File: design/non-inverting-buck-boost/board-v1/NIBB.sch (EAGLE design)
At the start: 0 parts

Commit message: added switches
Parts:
- added D1, D2: MUR820, diode:MUR820
- added L1: RKE16, inductors:RKE16
- added Q1, Q2: IRLZ44Z, transistor-power:IRLZ44Z
- added U$1: ZXGD3006E6, felippe:ZXGD3006E6
- added VIN: 2PIN, con-molex:22-23-2021
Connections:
- new net N$1: D1.C, L1.1, Q1.S
- new net N$2: L1.2, Q2.D
- new net N$3: Q1.D, VIN-1.S
- new net N$4: D1.A, Q2.S, VIN-2.S

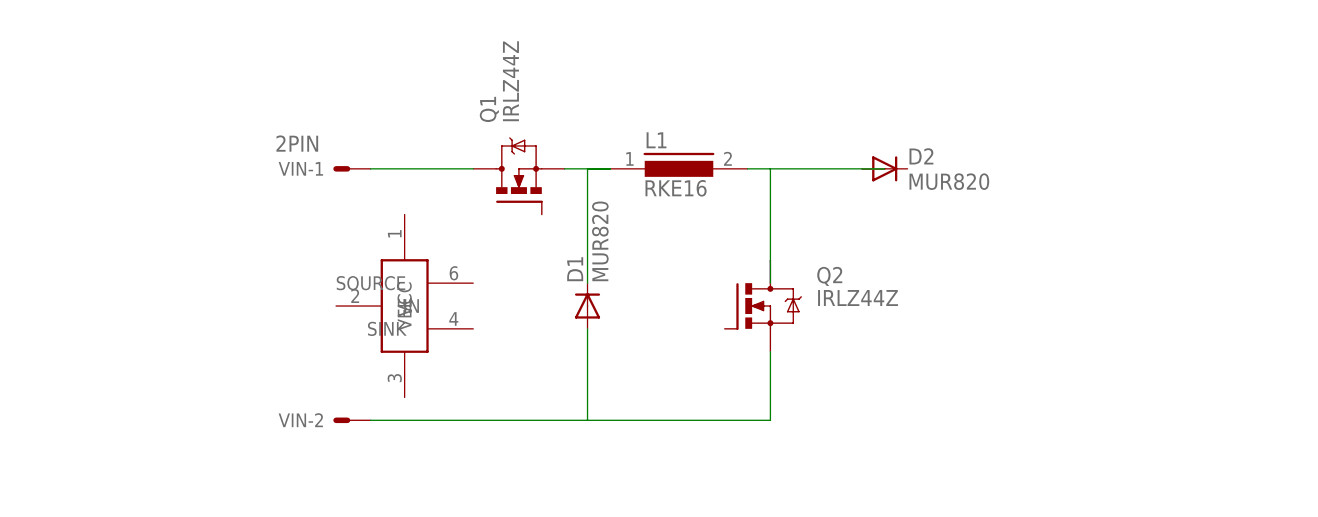
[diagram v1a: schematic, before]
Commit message: added connectors
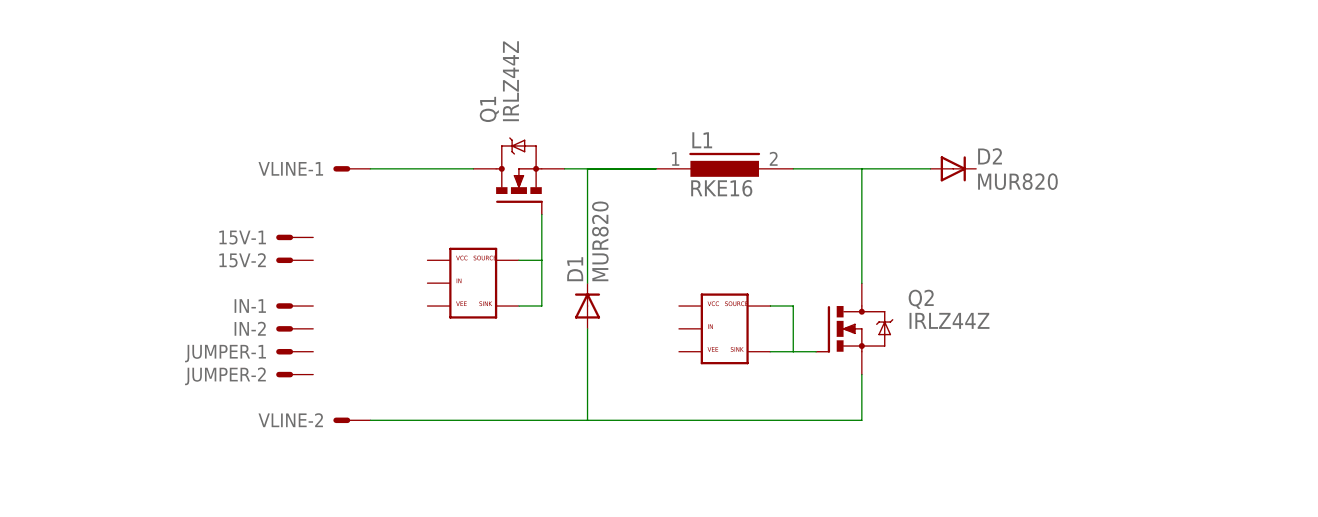
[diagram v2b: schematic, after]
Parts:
- added 15V, IN, JUMPER: 22-23-2021, con-molex:22-23-2021
- added U$2: ZXGD3006E6, felippe:ZXGD3006E6
- VLINE: value 2PIN -> 22-23-2021
- renumbered VIN to VLINE
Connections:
- new net N$5: Q1.G, U$1.SINK, U$1.SOURCE
- new net N$6: Q2.G, U$2.SINK, U$2.SOURCE
- net N$2: now also D2.A
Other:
- moved on the sheet: D2, L1, Q2
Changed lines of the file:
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@@
 <part name="L1" library="inductors" deviceset="RKE16" device=""/>
 <part name="Q2" library="transistor-power" deviceset="IRLZ44Z" device=""/>
-<part name="VIN" library="con-molex" deviceset="22-23-2021" device="" value="2PIN"/>
+<part name="VLINE" library="con-molex" deviceset="22-23-2021" device="" value=""/>
 <part name="U$1" library="felippe" deviceset="ZXGD3006E6" device=""/>
+<part name="U$2" library="felippe" deviceset="ZXGD3006E6" device=""/>
+<part name="15V" library="con-molex" deviceset="22-23-2021" device="" value=""/>
+<part name="IN" library="con-molex" deviceset="22-23-2021" device="" value=""/>
+<part name="JUMPER" library="con-molex" deviceset="22-23-2021" device="" value=""/>
 </parts>
 <sheets>
@@
 <instances>
 <instance part="D1" gate="1" x="25.4" y="48.26" rot="R90"/>
-<instance part="D2" gate="1" x="58.42" y="63.5"/>
+<instance part="D2" gate="1" x="66.04" y="63.5"/>
 <instance part="Q1" gate="G$1" x="17.78" y="60.96" rot="R90"/>
-<instance part="L1" gate="1" x="35.56" y="63.5"/>
-<instance part="Q2" gate="G$1" x="43.18" y="48.26"/>
-<instance part="VIN" gate="-1" x="-1.27" y="63.5" smashed="yes" rot="R180">
-<attribute name="NAME" x="-3.81" y="64.262" size="1.524" layer="95" rot="R180"/>
-<attribute name="VALUE" x="-4.318" y="67.183" size="1.778" layer="96" rot="R180"/>
+<instance part="L1" gate="1" x="40.64" y="63.5"/>
+<instance part="Q2" gate="G$1" x="53.34" y="45.72"/>
+<instance part="VLINE" gate="-1" x="-1.27" y="63.5" rot="R180"/>
+<instance part="VLINE" gate="-2" x="-1.27" y="35.56" rot="R180"/>
+<instance part="U$1" gate="G$1" x="12.7" y="50.8"/>
+<instance part="U$2" gate="G$1" x="40.64" y="45.72"/>
+<instance part="15V" gate="-1" x="-7.62" y="55.88" smashed="yes" rot="R180">
+<attribute name="NAME" x="-10.16" y="56.642" size="1.524" layer="95" rot="R180"/>
+<attribute name="VALUE" x="-11.938" y="59.563" size="1.778" layer="96" rot="R180"/>
 </instance>
-<instance part="VIN" gate="-2" x="-1.27" y="35.56" rot="R180"/>
-<instance part="U$1" gate="G$1" x="5.08" y="48.26"/>
+<instance part="15V" gate="-2" x="-7.62" y="53.34" rot="R180"/>
+<instance part="IN" gate="-1" x="-7.62" y="48.26" smashed="yes" rot="R180">
+<attribute name="NAME" x="-10.16" y="49.022" size="1.524" layer="95" rot="R180"/>
+<attribute name="VALUE" x="-11.938" y="51.943" size="1.778" layer="96" rot="R180"/>
+</instance>
+<instance part="IN" gate="-2" x="-7.62" y="45.72" rot="R180"/>
+<instance part="JUMPER" gate="-1" x="-7.62" y="43.18" rot="R180"/>
+<instance part="JUMPER" gate="-2" x="-7.62" y="40.64" rot="R180"/>
 </instances>
 <busses>
@@
 <pinref part="Q1" gate="G$1" pin="S"/>
 <pinref part="L1" gate="1" pin="1"/>
-<wire x1="22.86" y1="63.5" x2="27.94" y2="63.5" width="0.1524" layer="91"/>
-<wire x1="27.94" y1="63.5" x2="25.4" y2="63.5" width="0.1524" layer="91"/>
+<wire x1="22.86" y1="63.5" x2="33.02" y2="63.5" width="0.1524" layer="91"/>
+<wire x1="33.02" y1="63.5" x2="25.4" y2="63.5" width="0.1524" layer="91"/>
 <wire x1="25.4" y1="63.5" x2="25.4" y2="50.8" width="0.1524" layer="91"/>
 <pinref part="D1" gate="1" pin="C"/>
@@
 <segment>
 <pinref part="Q2" gate="G$1" pin="D"/>
-<wire x1="45.72" y1="53.34" x2="45.72" y2="50.8" width="0.1524" layer="91"/>
 <pinref part="L1" gate="1" pin="2"/>
-<wire x1="43.18" y1="63.5" x2="45.72" y2="63.5" width="0.1524" layer="91"/>
-<wire x1="45.72" y1="63.5" x2="58.42" y2="63.5" width="0.1524" layer="91"/>
-<wire x1="45.72" y1="53.34" x2="45.72" y2="63.5" width="0.1524" layer="91"/>
+<wire x1="48.26" y1="63.5" x2="55.88" y2="63.5" width="0.1524" layer="91"/>
+<wire x1="55.88" y1="50.8" x2="55.88" y2="63.5" width="0.1524" layer="91"/>
+<pinref part="D2" gate="1" pin="A"/>
+<wire x1="55.88" y1="63.5" x2="63.5" y2="63.5" width="0.1524" layer="91"/>
 </segment>
 </net>
@@
 <segment>
 <pinref part="Q2" gate="G$1" pin="S"/>
-<wire x1="45.72" y1="43.18" x2="45.72" y2="35.56" width="0.1524" layer="91"/>
-<wire x1="45.72" y1="35.56" x2="25.4" y2="35.56" width="0.1524" layer="91"/>
+<wire x1="55.88" y1="40.64" x2="55.88" y2="35.56" width="0.1524" layer="91"/>
+<wire x1="55.88" y1="35.56" x2="25.4" y2="35.56" width="0.1524" layer="91"/>
 <pinref part="D1" gate="1" pin="A"/>
 <wire x1="25.4" y1="35.56" x2="25.4" y2="45.72" width="0.1524" layer="91"/>
-<pinref part="VIN" gate="-2" pin="S"/>
+<pinref part="VLINE" gate="-2" pin="S"/>
 <wire x1="1.27" y1="35.56" x2="25.4" y2="35.56" width="0.1524" layer="91"/>
 </segment>
@@
 <segment>
 <pinref part="Q1" gate="G$1" pin="D"/>
-<pinref part="VIN" gate="-1" pin="S"/>
+<pinref part="VLINE" gate="-1" pin="S"/>
 <wire x1="1.27" y1="63.5" x2="12.7" y2="63.5" width="0.1524" layer="91"/>
 </segment>
 </net>
+<net name="N$5" class="0">
+<segment>
+<pinref part="U$1" gate="G$1" pin="SOURCE"/>
+<wire x1="17.78" y1="53.34" x2="20.32" y2="53.34" width="0.1524" layer="91"/>
+<pinref part="Q1" gate="G$1" pin="G"/>
+<wire x1="20.32" y1="53.34" x2="20.32" y2="58.42" width="0.1524" layer="91"/>
+<pinref part="U$1" gate="G$1" pin="SINK"/>
+<wire x1="17.78" y1="48.26" x2="20.32" y2="48.26" width="0.1524" layer="91"/>
+<wire x1="20.32" y1="48.26" x2="20.32" y2="53.34" width="0.1524" layer="91"/>
+</segment>
+</net>
+<net name="N$6" class="0">
+<segment>
+<pinref part="U$2" gate="G$1" pin="SOURCE"/>
+<wire x1="48.26" y1="48.26" x2="45.72" y2="48.26" width="0.1524" layer="91"/>
+<wire x1="48.26" y1="43.18" x2="48.26" y2="48.26" width="0.1524" layer="91"/>
+<pinref part="U$2" gate="G$1" pin="SINK"/>
+<wire x1="45.72" y1="43.18" x2="48.26" y2="43.18" width="0.1524" layer="91"/>
+<pinref part="Q2" gate="G$1" pin="G"/>
+<wire x1="48.26" y1="43.18" x2="50.8" y2="43.18" width="0.1524" layer="91"/>
+</segment>
+</net>

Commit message: updated connectors
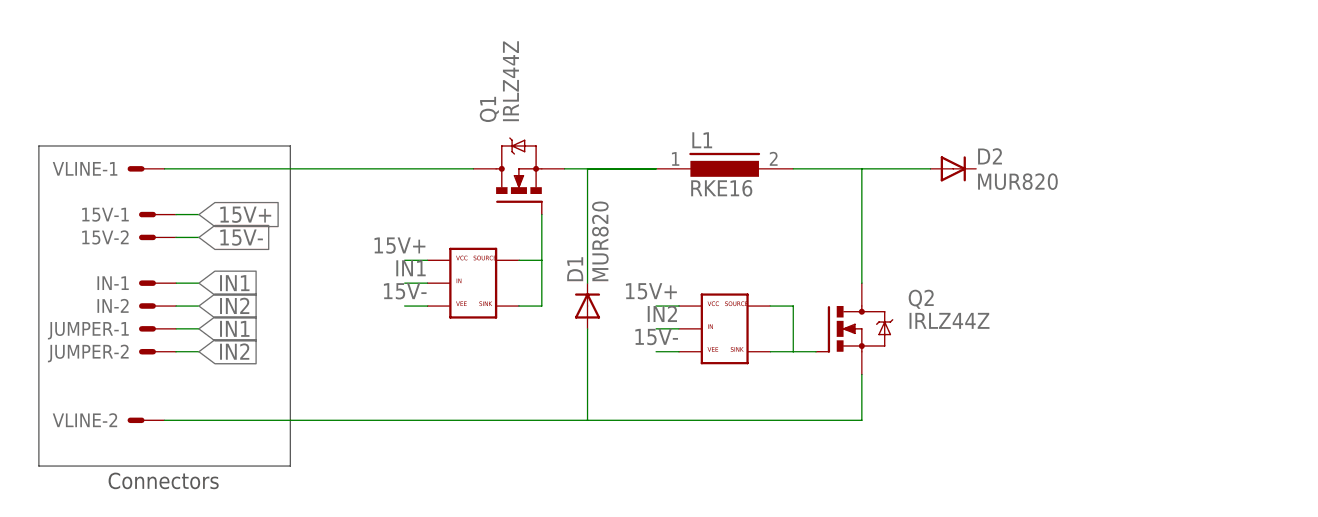
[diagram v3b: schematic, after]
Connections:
- new net 15V+: 15V-1.S, U$1.VCC, U$2.VCC
- new net 15V-: 15V-2.S, U$1.VEE, U$2.VEE
- new net IN1: IN-1.S, JUMPER-1.S, U$1.IN
- new net IN2: IN-2.S, JUMPER-2.S, U$2.IN
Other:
- note added: "Connectors"
- moved on the sheet: 15V-1, 15V-2, IN-1, IN-2, JUMPER-1, JUMPER-2, VLINE-1, VLINE-2
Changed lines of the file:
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@@
 <sheet>
 <plain>
+<text x="-27.94" y="27.94" size="1.778" layer="92">Connectors</text>
 </plain>
 <instances>
@@
 <instance part="L1" gate="1" x="40.64" y="63.5"/>
 <instance part="Q2" gate="G$1" x="53.34" y="45.72"/>
-<instance part="VLINE" gate="-1" x="-1.27" y="63.5" rot="R180"/>
-<instance part="VLINE" gate="-2" x="-1.27" y="35.56" rot="R180"/>
+<instance part="VLINE" gate="-1" x="-24.13" y="63.5" rot="R180"/>
+<instance part="VLINE" gate="-2" x="-24.13" y="35.56" rot="R180"/>
 <instance part="U$1" gate="G$1" x="12.7" y="50.8"/>
 <instance part="U$2" gate="G$1" x="40.64" y="45.72"/>
-<instance part="15V" gate="-1" x="-7.62" y="55.88" smashed="yes" rot="R180">
-<attribute name="NAME" x="-10.16" y="56.642" size="1.524" layer="95" rot="R180"/>
-<attribute name="VALUE" x="-11.938" y="59.563" size="1.778" layer="96" rot="R180"/>
+<instance part="15V" gate="-1" x="-22.86" y="58.42" smashed="yes" rot="R180">
+<attribute name="NAME" x="-25.4" y="59.182" size="1.524" layer="95" rot="R180"/>
+<attribute name="VALUE" x="-27.178" y="62.103" size="1.778" layer="96" rot="R180"/>
 </instance>
-<instance part="15V" gate="-2" x="-7.62" y="53.34" rot="R180"/>
-<instance part="IN" gate="-1" x="-7.62" y="48.26" smashed="yes" rot="R180">
-<attribute name="NAME" x="-10.16" y="49.022" size="1.524" layer="95" rot="R180"/>
-<attribute name="VALUE" x="-11.938" y="51.943" size="1.778" layer="96" rot="R180"/>
+<instance part="15V" gate="-2" x="-22.86" y="55.88" rot="R180"/>
+<instance part="IN" gate="-1" x="-22.86" y="50.8" smashed="yes" rot="R180">
+<attribute name="NAME" x="-25.4" y="51.562" size="1.524" layer="95" rot="R180"/>
+<attribute name="VALUE" x="-27.178" y="54.483" size="1.778" layer="96" rot="R180"/>
 </instance>
-<instance part="IN" gate="-2" x="-7.62" y="45.72" rot="R180"/>
-<instance part="JUMPER" gate="-1" x="-7.62" y="43.18" rot="R180"/>
-<instance part="JUMPER" gate="-2" x="-7.62" y="40.64" rot="R180"/>
+<instance part="IN" gate="-2" x="-22.86" y="48.26" rot="R180"/>
+<instance part="JUMPER" gate="-1" x="-22.86" y="45.72" rot="R180"/>
+<instance part="JUMPER" gate="-2" x="-22.86" y="43.18" rot="R180"/>
 </instances>
 <busses>
+<bus name="B$1">
+<segment>
+<wire x1="-35.56" y1="66.04" x2="-7.62" y2="66.04" width="0.762" layer="92"/>
+<wire x1="-7.62" y1="66.04" x2="-7.62" y2="30.48" width="0.762" layer="92"/>
+<wire x1="-7.62" y1="30.48" x2="-35.56" y2="30.48" width="0.762" layer="92"/>
+<wire x1="-35.56" y1="30.48" x2="-35.56" y2="66.04" width="0.762" layer="92"/>
+</segment>
+</bus>
 </busses>
 <nets>
@@
 <wire x1="25.4" y1="35.56" x2="25.4" y2="45.72" width="0.1524" layer="91"/>
 <pinref part="VLINE" gate="-2" pin="S"/>
-<wire x1="1.27" y1="35.56" x2="25.4" y2="35.56" width="0.1524" layer="91"/>
+<wire x1="-21.59" y1="35.56" x2="25.4" y2="35.56" width="0.1524" layer="91"/>
 </segment>
 </net>
@@
 <pinref part="Q1" gate="G$1" pin="D"/>
 <pinref part="VLINE" gate="-1" pin="S"/>
-<wire x1="1.27" y1="63.5" x2="12.7" y2="63.5" width="0.1524" layer="91"/>
+<wire x1="-21.59" y1="63.5" x2="12.7" y2="63.5" width="0.1524" layer="91"/>
 </segment>
 </net>
@@
 </segment>
 </net>
+<net name="15V+" class="0">
+<segment>
+<pinref part="15V" gate="-1" pin="S"/>
+<wire x1="-20.32" y1="58.42" x2="-17.78" y2="58.42" width="0.1524" layer="91"/>
+<label x="-17.78" y="58.42" size="1.778" layer="95" xref="yes"/>
+</segment>
+<segment>
+<pinref part="U$1" gate="G$1" pin="VCC"/>
+<wire x1="7.62" y1="53.34" x2="5.08" y2="53.34" width="0.1524" layer="91"/>
+<label x="7.62" y="55.88" size="1.778" layer="95" rot="R180"/>
+</segment>
+<segment>
+<pinref part="U$2" gate="G$1" pin="VCC"/>
+<wire x1="35.56" y1="48.26" x2="33.02" y2="48.26" width="0.1524" layer="91"/>
+<label x="35.56" y="50.8" size="1.778" layer="95" rot="R180"/>
+</segment>
+</net>
+<net name="15V-" class="0">
+<segment>
+<pinref part="15V" gate="-2" pin="S"/>
+<wire x1="-20.32" y1="55.88" x2="-17.78" y2="55.88" width="0.1524" layer="91"/>
+<label x="-17.78" y="55.88" size="1.778" layer="95" xref="yes"/>
+</segment>
+<segment>
+<pinref part="U$1" gate="G$1" pin="VEE"/>
+<wire x1="7.62" y1="48.26" x2="5.08" y2="48.26" width="0.1524" layer="91"/>
+<label x="7.62" y="50.8" size="1.778" layer="95" rot="R180"/>
+</segment>
+<segment>
+<pinref part="U$2" gate="G$1" pin="VEE"/>
+<wire x1="35.56" y1="43.18" x2="33.02" y2="43.18" width="0.1524" layer="91"/>
+<label x="35.56" y="45.72" size="1.778" layer="95" rot="R180"/>
+</segment>
+</net>
+<net name="IN1" class="0">
+<segment>
+<pinref part="IN" gate="-1" pin="S"/>
+<wire x1="-20.32" y1="50.8" x2="-17.78" y2="50.8" width="0.1524" layer="91"/>
+<label x="-17.78" y="50.8" size="1.778" layer="95" xref="yes"/>
+</segment>
+<segment>
+<pinref part="JUMPER" gate="-1" pin="S"/>
+<wire x1="-20.32" y1="45.72" x2="-17.78" y2="45.72" width="0.1524" layer="91"/>
+<label x="-17.78" y="45.72" size="1.778" layer="95" xref="yes"/>
+</segment>
+<segment>
+<pinref part="U$1" gate="G$1" pin="IN"/>
+<wire x1="7.62" y1="50.8" x2="5.08" y2="50.8" width="0.1524" layer="91"/>
+<label x="7.62" y="53.34" size="1.778" layer="95" rot="R180"/>
+</segment>
+</net>
+<net name="IN2" class="0">
+<segment>
+<pinref part="IN" gate="-2" pin="S"/>
+<wire x1="-20.32" y1="48.26" x2="-17.78" y2="48.26" width="0.1524" layer="91"/>
+<label x="-17.78" y="48.26" size="1.778" layer="95" xref="yes"/>
+</segment>
+<segment>
+<pinref part="JUMPER" gate="-2" pin="S"/>
+<wire x1="-20.32" y1="43.18" x2="-17.78" y2="43.18" width="0.1524" layer="91"/>
+<label x="-17.78" y="43.18" size="1.778" layer="95" xref="yes"/>
+</segment>
+<segment>
+<pinref part="U$2" gate="G$1" pin="IN"/>
+<wire x1="35.56" y1="45.72" x2="33.02" y2="45.72" width="0.1524" layer="91"/>
+<label x="35.56" y="48.26" size="1.778" layer="95" rot="R180"/>
+</segment>
+</net>

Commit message: added output capacitor and connector
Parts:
- added C1: (no value), capacitor:CAPP-UF
- added OUT: 22-23-2021, con-molex:22-23-2021
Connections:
- new net N$7: C1.+, D2.C, OUT-1.S
- net N$4: now also C1.-, OUT-2.S
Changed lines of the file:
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@@
 <part name="IN" library="con-molex" deviceset="22-23-2021" device="" value=""/>
 <part name="JUMPER" library="con-molex" deviceset="22-23-2021" device="" value=""/>
+<part name="C1" library="capacitor" deviceset="CAPP-U" device="F"/>
+<part name="OUT" library="con-molex" deviceset="22-23-2021" device="" value=""/>
 </parts>
 <sheets>
@@
 <instance part="JUMPER" gate="-1" x="-22.86" y="45.72" rot="R180"/>
 <instance part="JUMPER" gate="-2" x="-22.86" y="43.18" rot="R180"/>
+<instance part="C1" gate="G$1" x="81.28" y="48.26"/>
+<instance part="OUT" gate="-1" x="93.98" y="63.5" smashed="yes">
+<attribute name="NAME" x="96.52" y="62.738" size="1.524" layer="95"/>
+<attribute name="VALUE" x="98.298" y="59.817" size="1.778" layer="96"/>
+</instance>
+<instance part="OUT" gate="-2" x="93.98" y="35.56"/>
 </instances>
 <busses>
@@
 </busses>
 <nets>
-<net name="N$1" class="0">
-<segment>
-<pinref part="Q1" gate="G$1" pin="S"/>
-<pinref part="L1" gate="1" pin="1"/>
-<wire x1="22.86" y1="63.5" x2="33.02" y2="63.5" width="0.1524" layer="91"/>
-<wire x1="33.02" y1="63.5" x2="25.4" y2="63.5" width="0.1524" layer="91"/>
-<wire x1="25.4" y1="63.5" x2="25.4" y2="50.8" width="0.1524" layer="91"/>
-<pinref part="D1" gate="1" pin="C"/>
-</segment>
-</net>
 <net name="N$2" class="0">
 <segment>
+<pinref part="L1" gate="1" pin="2"/>
+<pinref part="D2" gate="1" pin="A"/>
+<wire x1="48.26" y1="63.5" x2="55.88" y2="63.5" width="0.1524" layer="91"/>
 <pinref part="Q2" gate="G$1" pin="D"/>
-<pinref part="L1" gate="1" pin="2"/>
-<wire x1="48.26" y1="63.5" x2="55.88" y2="63.5" width="0.1524" layer="91"/>
+<wire x1="55.88" y1="63.5" x2="63.5" y2="63.5" width="0.1524" layer="91"/>
 <wire x1="55.88" y1="50.8" x2="55.88" y2="63.5" width="0.1524" layer="91"/>
-<pinref part="D2" gate="1" pin="A"/>
-<wire x1="55.88" y1="63.5" x2="63.5" y2="63.5" width="0.1524" layer="91"/>
+<junction x="55.88" y="63.5"/>
 </segment>
 </net>
@@
 <pinref part="Q2" gate="G$1" pin="S"/>
 <wire x1="55.88" y1="40.64" x2="55.88" y2="35.56" width="0.1524" layer="91"/>
-<wire x1="55.88" y1="35.56" x2="25.4" y2="35.56" width="0.1524" layer="91"/>
-<pinref part="D1" gate="1" pin="A"/>
-<wire x1="25.4" y1="35.56" x2="25.4" y2="45.72" width="0.1524" layer="91"/>
 <pinref part="VLINE" gate="-2" pin="S"/>
 <wire x1="-21.59" y1="35.56" x2="25.4" y2="35.56" width="0.1524" layer="91"/>
+<pinref part="C1" gate="G$1" pin="-"/>
+<wire x1="25.4" y1="35.56" x2="55.88" y2="35.56" width="0.1524" layer="91"/>
+<wire x1="81.28" y1="45.72" x2="81.28" y2="35.56" width="0.1524" layer="91"/>
+<wire x1="81.28" y1="35.56" x2="55.88" y2="35.56" width="0.1524" layer="91"/>
+<junction x="55.88" y="35.56"/>
+<pinref part="D1" gate="1" pin="A"/>
+<wire x1="25.4" y1="45.72" x2="25.4" y2="35.56" width="0.1524" layer="91"/>
+<junction x="25.4" y="35.56"/>
+<pinref part="OUT" gate="-2" pin="S"/>
+<wire x1="91.44" y1="35.56" x2="81.28" y2="35.56" width="0.1524" layer="91"/>
+<junction x="81.28" y="35.56"/>
 </segment>
 </net>
@@
 </segment>
 </net>
+<net name="N$7" class="0">
+<segment>
+<pinref part="D2" gate="1" pin="C"/>
+<wire x1="68.58" y1="63.5" x2="81.28" y2="63.5" width="0.1524" layer="91"/>
+<wire x1="81.28" y1="63.5" x2="81.28" y2="50.8" width="0.1524" layer="91"/>
+<pinref part="C1" gate="G$1" pin="+"/>
+<pinref part="OUT" gate="-1" pin="S"/>
+<wire x1="91.44" y1="63.5" x2="81.28" y2="63.5" width="0.1524" layer="91"/>
+<junction x="81.28" y="63.5"/>
+</segment>
+</net>
+<net name="N$1" class="0">
+<segment>
+<pinref part="Q1" gate="G$1" pin="S"/>
+<pinref part="L1" gate="1" pin="1"/>
+<wire x1="22.86" y1="63.5" x2="25.4" y2="63.5" width="0.1524" layer="91"/>
+<pinref part="D1" gate="1" pin="C"/>
+<wire x1="25.4" y1="63.5" x2="33.02" y2="63.5" width="0.1524" layer="91"/>
+<wire x1="25.4" y1="50.8" x2="25.4" y2="63.5" width="0.1524" layer="91"/>
+<junction x="25.4" y="63.5"/>
+</segment>
+</net>
